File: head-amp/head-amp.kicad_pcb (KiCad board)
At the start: 2 copper layers, 38 x 52 mm, 33 parts, among them IC1 OPA1642AID

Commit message: Finished head amp PCB layout, generated gerber + BOM
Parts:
- added REF**: VOROX_logo, 01_Custom:VOROX_logo, B.Cu at (79.5, 74.5)
- BACKPLATE: renamed from BCKPLT; footprint Connector_Wire:SolderWire-0.1sqmm_1x01_D0.4mm_OD1mm -> Connector_Wire:SolderWire-0.25sqmm_1x01_D0.65mm_OD2mm
- SIGNAL: renamed from SGNL; footprint Connector_Wire:SolderWire-0.1sqmm_1x01_D0.4mm_OD1mm -> Connector_Wire:SolderWire-0.25sqmm_1x01_D0.65mm_OD2mm
- XLR1, XLR2, XLR3: footprint Connector_Wire:SolderWire-0.1sqmm_1x01_D0.4mm_OD1mm -> Connector_Wire:SolderWire-0.25sqmm_1x01_D0.65mm_OD2mm
- moved C6 0.75 mm to (71.5, 52.5)
- moved VCC2 0.75 mm to (75.5, 54.2)
- moved D1 0.50 mm to (52.0, 74.5)
- moved R4 0.50 mm to (55.0, 74.5)
- renumbered TP_GND to GND1, TP_VCC to VCC1, TP_VCC2 to VCC2
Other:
- board text added: "A U D I O"
- board text added: "BACKPLATE"
- board text added: "Microphone Head-Amp v1.0"
- board text added: "Options for capsule resistor: 1) 1Gig through-hole (R5) 2) 1Gig SMD_1206 (R5) 3) 10x 100M (R6-R15) Choose only one, leave others unpopulated!"
- board text added: "SIGNAL"
- board text added: "XLR1"
- board text added: "XLR2"
- board text added: "XLR3"

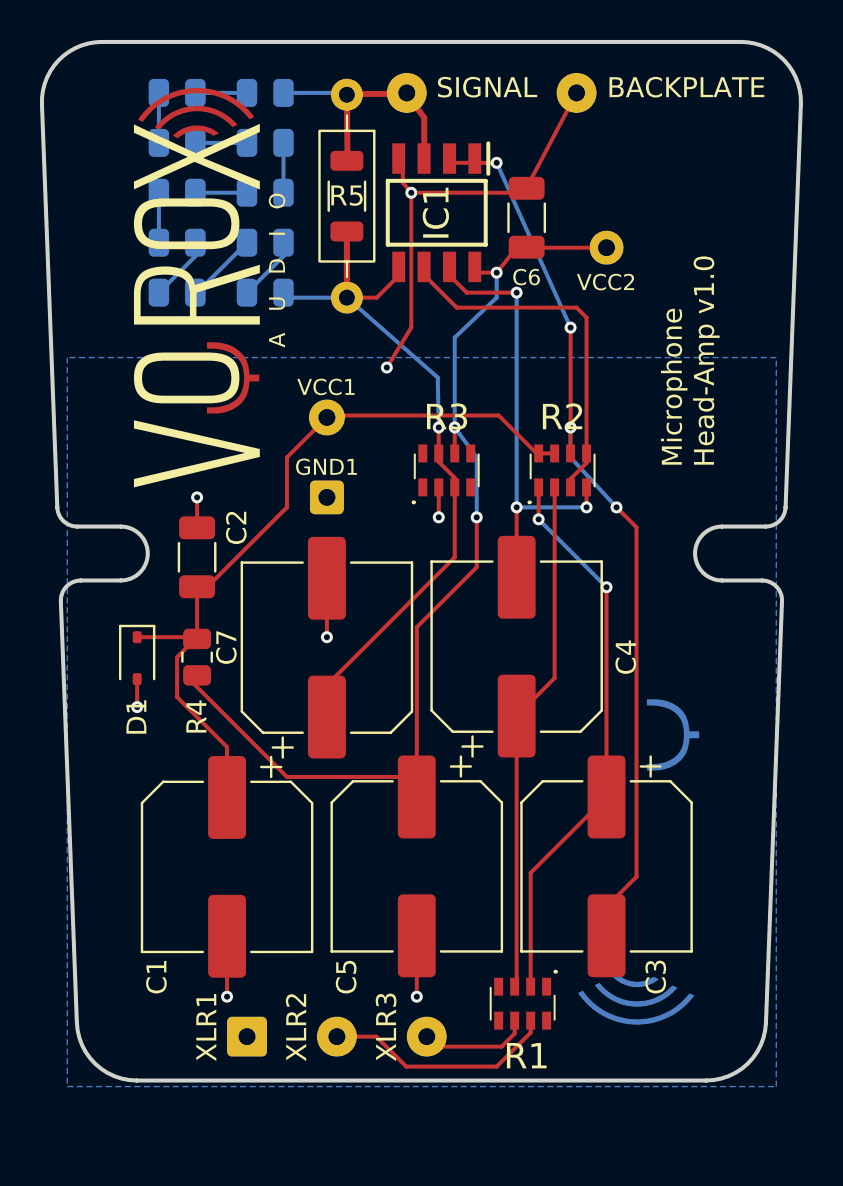
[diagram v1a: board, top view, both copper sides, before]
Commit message: Added kikit panel files for two completed projects
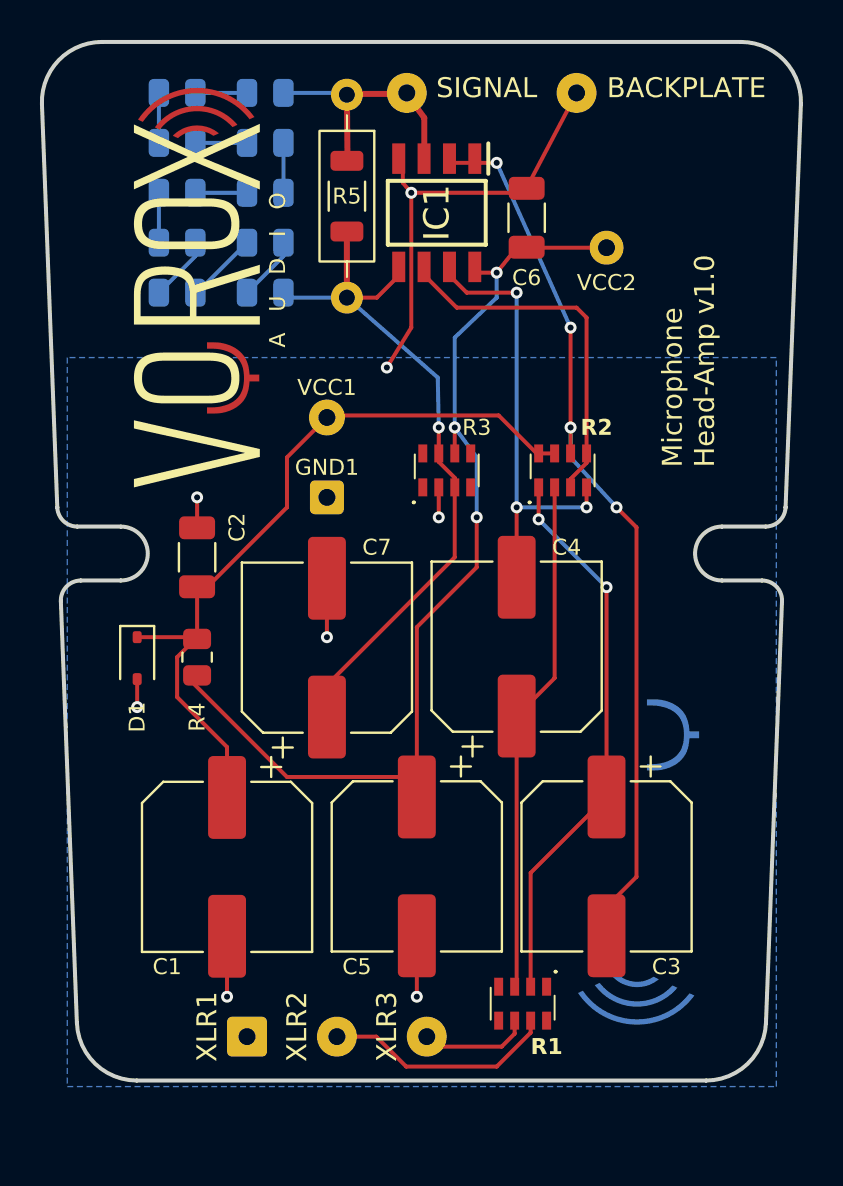
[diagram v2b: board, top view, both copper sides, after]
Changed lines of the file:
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@@
 		(tags "capacitor electrolytic")
 		(property "Reference" "C4"
-			(at -0.525 5.5 270)
+			(at 4.975 2.5 0)
 			(layer "F.SilkS")
 			(effects
 				(font
-					(size 1 1)
+					(size 0.8 0.8)
 					(thickness 0.15)
 				)
@@
 		(tags "Resistor Network")
 		(property "Reference" "R3"
-			(at 0 -2.65 0)
+			(at 1.5 -2.15 0)
 			(layer "F.SilkS")
 			(effects
 				(font
-					(size 1.27 1.27)
-					(thickness 0.254)
+					(size 0.8 0.8)
+					(thickness 0.15)
 				)
 			)
@@
 			(effects
 				(font
-					(size 1 1)
+					(size 0.8 0.8)
 					(thickness 0.15)
 				)
@@
 			(effects
 				(font
-					(size 1 1)
+					(size 0.8 0.8)
 					(thickness 0.15)
 				)
@@
 		(tags "Resistor Network")
 		(property "Reference" "R1"
-			(at -0.2 -2.65 0)
+			(at -1.2 -2.15 0)
 			(layer "F.SilkS")
 			(effects
 				(font
-					(size 1.27 1.27)
-					(thickness 0.254)
+					(size 0.8 0.8)
+					(thickness 0.15)
+					(bold yes)
 				)
 			)
@@
 		(tags "capacitor electrolytic")
 		(property "Reference" "C3"
-			(at 5.525 -2.5 270)
+			(at 5.025 -3 0)
 			(layer "F.SilkS")
 			(effects
 				(font
-					(size 1 1)
+					(size 0.8 0.8)
 					(thickness 0.15)
 				)
@@
 		(tags "Resistor Network")
 		(property "Reference" "R2"
-			(at 0 -2.65 0)
+			(at 1.7 -2.15 0)
 			(layer "F.SilkS")
 			(effects
 				(font
-					(size 1.27 1.27)
-					(thickness 0.254)
+					(size 0.8 0.8)
+					(thickness 0.15)
+					(bold yes)
 				)
 			)
@@
 			(effects
 				(font
-					(size 1 1)
+					(size 0.8 0.8)
 					(thickness 0.15)
 				)
@@
 		(tags "capacitor electrolytic")
 		(property "Reference" "C5"
-			(at 5.525 3.5 270)
+			(at 5.025 3 0)
 			(layer "F.SilkS")
 			(effects
 				(font
-					(size 1 1)
+					(size 0.8 0.8)
 					(thickness 0.15)
 				)
@@
 		(tags "capacitor electrolytic")
 		(property "Reference" "C7"
-			(at 0.025 -5 270)
+			(at 5.025 2.5 0)
 			(layer "F.SilkS")
 			(effects
 				(font
-					(size 1 1)
+					(size 0.8 0.8)
 					(thickness 0.15)
 				)
@@
 		(tags "capacitor electrolytic")
 		(property "Reference" "C1"
-			(at 5.5 3.5 270)
+			(at 5 3 0)
 			(layer "F.SilkS")
 			(effects
 				(font
-					(size 1 1)
+					(size 0.8 0.8)
 					(thickness 0.15)
 				)
@@
 			(effects
 				(font
-					(size 1 1)
+					(size 0.8 0.8)
 					(thickness 0.15)
 				)

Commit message: input/output connectors moved to 2.54mm spacing. Improved clearance around screw slots.
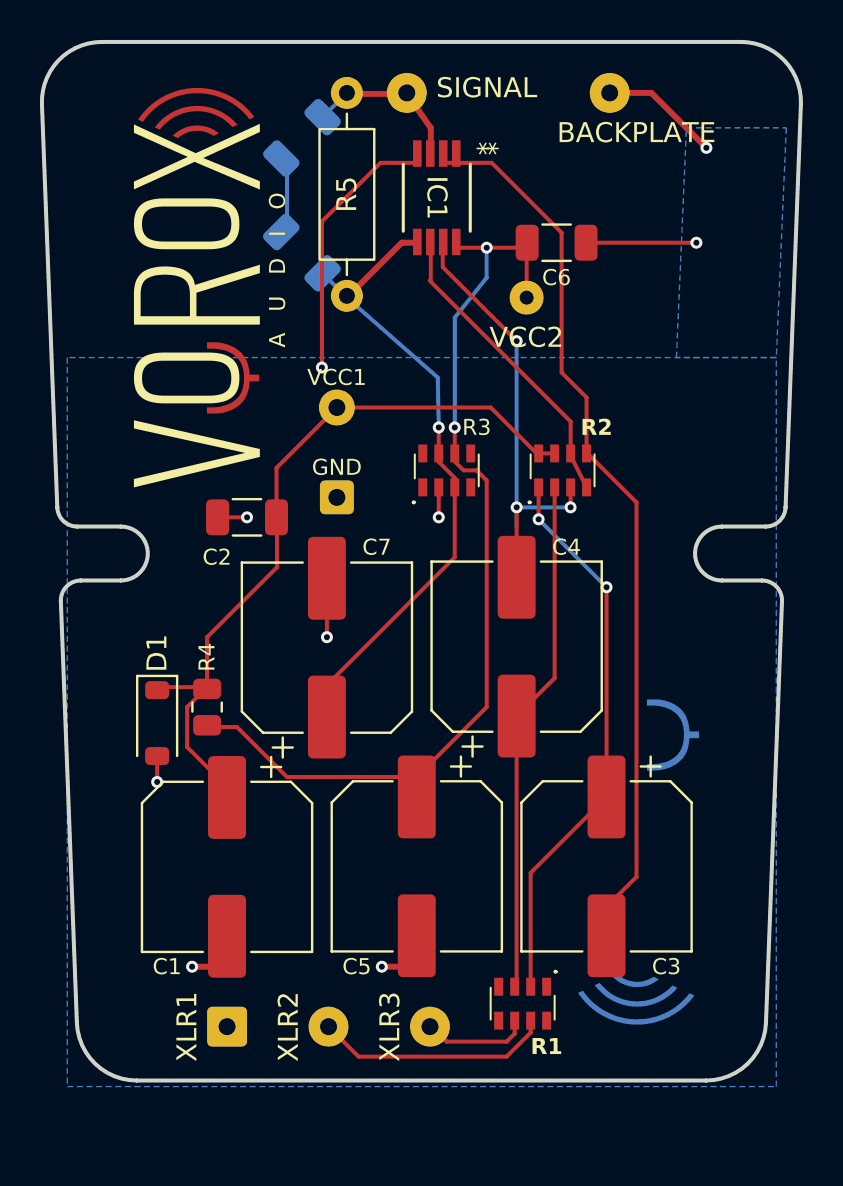
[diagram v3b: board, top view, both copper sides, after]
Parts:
- removed R10, R12, R13, R14, R15, R8, R9: 100M, Resistor_SMD:R_0805_2012Metric
- removed the R7 at (54.0, 46.2)
- D1: footprint Diode_SMD:D_SOD-323 -> Diode_SMD:D_SOD-123
- IC1: footprint 01_footprints-custom:SOIC127P600X175-8N -> OPA1642_VSSOP-8:DGK8
- R5: footprint 01_Custom:R_Axial_THT-SMD-Dual -> Resistor_THT:R_Axial_DIN0207_L6.3mm_D2.5mm_P10.16mm_Horizontal
- R6: value 100M -> 500M; footprint Resistor_SMD:R_0805_2012Metric -> Resistor_SMD:R_1206_3216Metric
- R7: renamed from R11; value 100M -> 500M; footprint Resistor_SMD:R_0805_2012Metric -> Resistor_SMD:R_1206_3216Metric
- moved VCC2 4.59 mm to (71.5, 56.5)
- moved D1 3.40 mm to (53.0, 77.8)
- moved C2 3.20 mm to (57.5, 67.5), turned to 180 degrees
- moved R6 2.90 mm to (60.2, 48.5), turned to -90 degrees
- moved R7 2.72 mm to (60.2, 54.2), turned to -90 degrees
- moved R4 2.55 mm to (55.5, 77.0)
- moved C6 1.95 mm to (73.0, 53.8), turned to 0 degrees
- moved BACKPLATE 1.66 mm to (75.7, 46.2)
- moved XLR1 1.12 mm to (56.5, 93.0)
- moved IC1 0.75 mm to (67.0, 51.5)
- moved VCC1 0.71 mm to (62.0, 62.0)
- moved XLR2 0.65 mm to (61.6, 93.0)
- moved XLR3 0.52 mm to (66.7, 93.0)
- moved GND 0.50 mm to (62.0, 66.5)
- moved R5 0.08 mm to (62.5, 46.2)
- renumbered GND1 to GND
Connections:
- R2 pad 3: Net-(IC1--IN_B) -> Net-(IC1-OUT_B)
- R2 pad 4: Net-(IC1-OUT_B) -> Net-(IC1--IN_B)
- R2 pad 5: Net-(IC1--IN_B) -> Net-(IC1--IN_A)
- R2 pad 6: Net-(IC1--IN_A) -> Net-(IC1--IN_B)
- R7 pad 1: Net-(IC1-+IN_B) -> Net-(R6-Pad2)
- R7 pad 2: Net-(R11-Pad2) -> Net-(IC1-+IN_B)
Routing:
- net Net-(IC1--IN_B): track 9.25 -> 0.00 mm
- net Net-(R12-Pad2): track 3.62 -> 0.00 mm
- net Net-(R13-Pad2): track 3.26 -> 0.00 mm
- net Net-(R11-Pad2): track 3.26 -> 0.00 mm
- net Net-(IC1-+IN_A): track 3.20 -> 0.06 mm
- net Net-(R8-Pad2): track 2.59 -> 0.00 mm
- net Net-(R6-Pad2): track 2.59 -> 0.00 mm
- net Net-(R10-Pad2): track 2.59 -> 0.00 mm
- net Net-(R7-Pad2): track 2.50 -> 0.00 mm
- net Net-(R14-Pad2): track 2.50 -> 0.00 mm
- net Net-(R10-Pad1): track 2.50 -> 0.00 mm
- net Net-(IC1--IN_A): track 1.30 -> 0.00 mm, vias 4 -> 0
- net Net-(D1-K): track 16.5 -> 17.6 mm
- net Net-(IC1-OUT_B): track 1.00 -> 0.00 mm
- net Net-(IC1-V+): vias 3 -> 2
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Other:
- board text added: "Microphone Head-Amp v1.1"
- board text added: "Options for capsule resistor: 1) 1Gig through-hole (R5) 2) 2x 500M SMD_1206 (R6, R7) Choose only one, leave others unpopulated!"
- board text removed: "Microphone Head-Amp v1.0"
- board text removed: "Options for capsule resistor: 1) 1Gig through-hole (R5) 2) 1Gig SMD_1206 (R5) 3) 10x 100M (R6-R15) Choose only one, leave others unpopulated!"
